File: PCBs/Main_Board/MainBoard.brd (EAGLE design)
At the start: 83.8 x 69.8 mm, 25 parts

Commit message: Minor changes to main board
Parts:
- moved USB_B 3.81 mm to (10.2, 57.1)
- moved USB_A 3.59 mm to (71.1, 61.0)
- moved R14 2.84 mm to (21.6, 52.1)
- moved R5 1.27 mm to (27.9, 24.1)
- moved 3.5MM 1.27 mm to (41.9, 59.7)
- flipped C1 to the top
- flipped C2 to the top
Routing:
- net GND: track 385.5 -> 360.5 mm
- net DAC_OUT: track 147.0 -> 154.2 mm
- net VCC_5: track 172.0 -> 177.9 mm
- net UART1_RX: track 59.3 -> 55.5 mm
- net LCD_MOSI: track 79.3 -> 75.6 mm
- net N$1: track 11.6 -> 14.8 mm
- net LCD_SCK: track 49.6 -> 46.9 mm
- net UART1_TX: track 60.9 -> 62.4 mm
- net LCD_CARD_CS: track 67.8 -> 66.3 mm
- net 3.5MM: track 20.8 -> 22.3 mm
- net LCD_MISO: track 58.9 -> 57.6 mm
- net N$6: track 3.81 -> 2.54 mm
- net ADDR_2: track 18.4 -> 17.4 mm

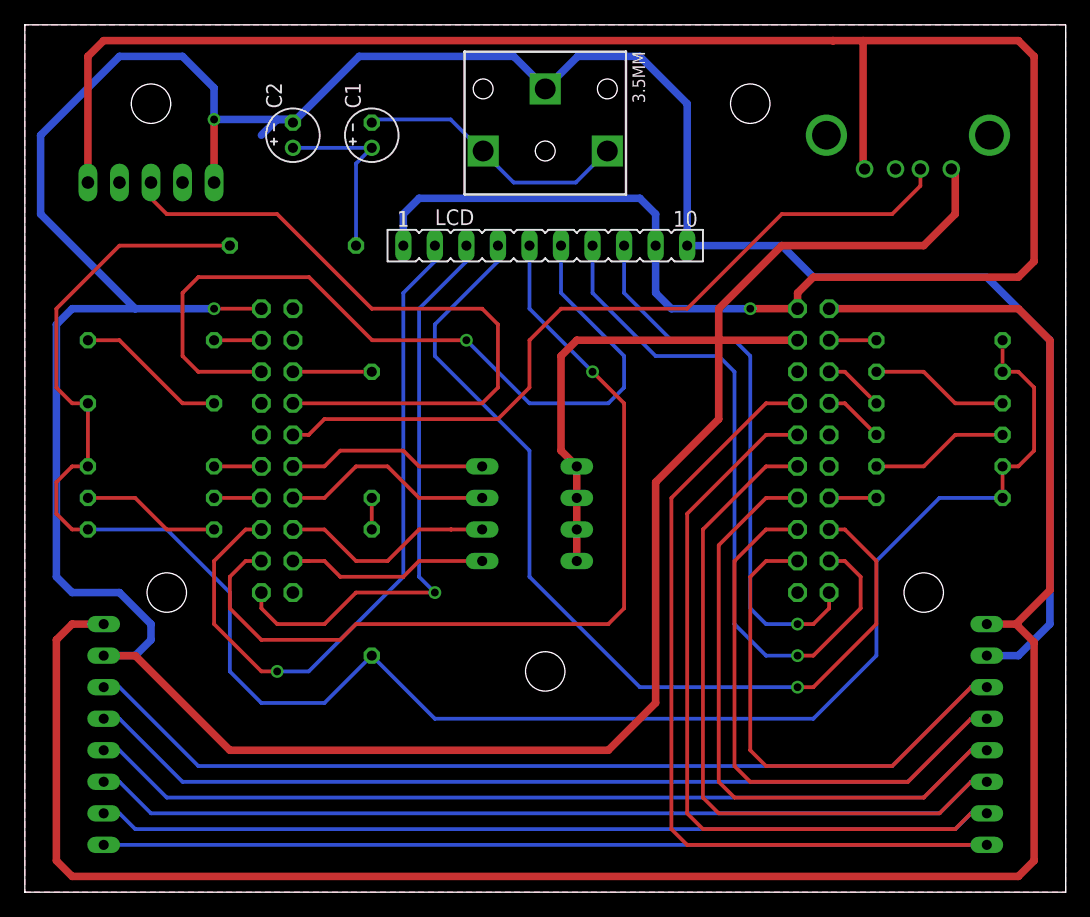
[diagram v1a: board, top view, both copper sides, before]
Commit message: Swapped D+/D- pins on the USB A port; misc optimizations
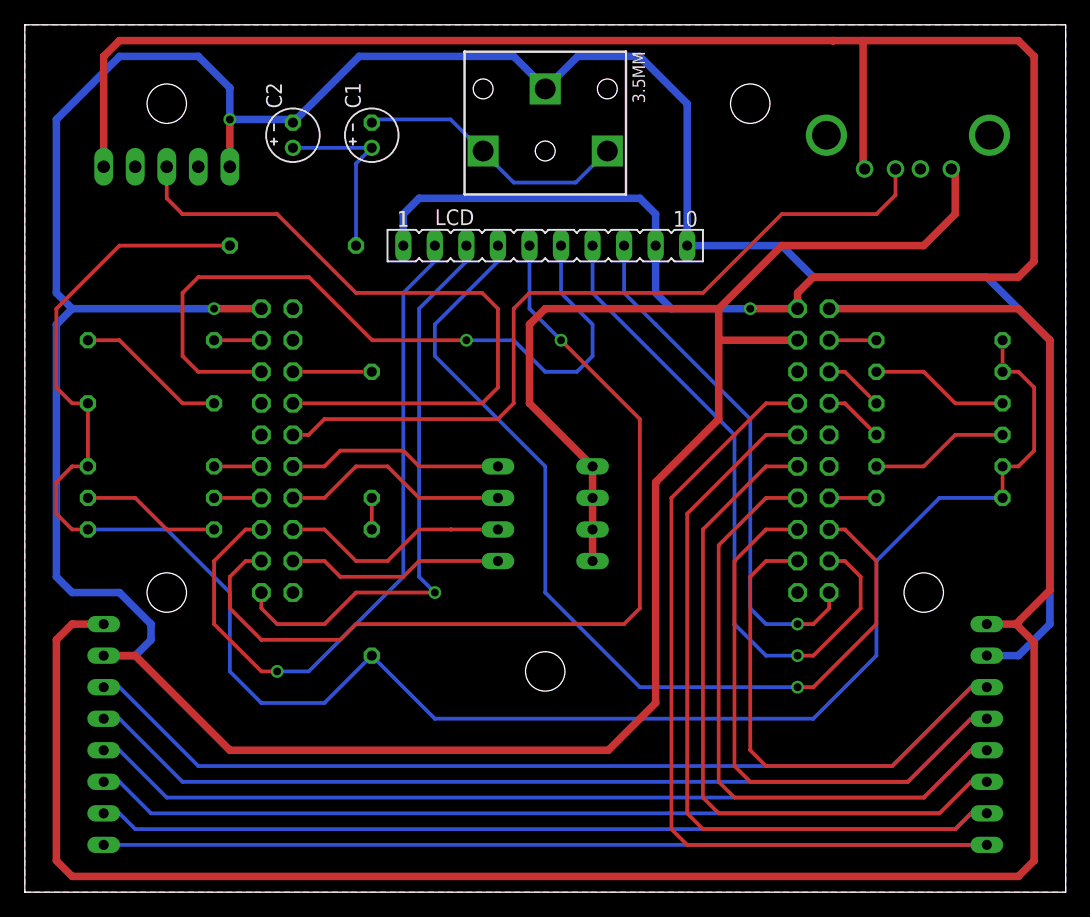
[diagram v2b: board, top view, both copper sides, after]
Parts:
- moved USB_B 1.80 mm to (11.4, 58.4)
- moved ADDR_SW 1.27 mm to (41.9, 30.5)
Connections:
- removed net N$67: USB_A.D-
- net UART1_TX: now also USB_A.D-; no longer USB_A.D+
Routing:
- net LCD_CARD_CS: track 66.3 -> 59.1 mm
- net LCD_D/C: track 56.6 -> 53.6 mm
- net LCD_RST: track 45.1 -> 42.1 mm
- net VCC_5: track 177.9 -> 175.4 mm
- net LCD_TFT_CS: track 71.8 -> 73.6 mm
- net ADDR_3: track 17.6 -> 18.8 mm
- net ADDR_1: track 17.3 -> 18.6 mm
- net ADDR_0: track 16.3 -> 17.6 mm
- net ADDR_2: track 17.4 -> 18.6 mm
- net UART1_RX: track 55.5 -> 56.3 mm
- net UART1_TX: track 62.4 -> 63.1 mm
- net GND: track 360.5 -> 359.9 mm

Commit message: Undid swap
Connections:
- net UART1_TX: now also USB_A.D+; no longer USB_A.D-
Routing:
- net UART1_TX: track 63.1 -> 65.4 mm
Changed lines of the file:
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@@
 <wire x1="54.61" y1="48.26" x2="60.96" y2="54.61" width="0.3048" layer="1"/>
 <wire x1="39.37" y1="39.37" x2="39.37" y2="46.99" width="0.3048" layer="1"/>
-<contactref element="USB_A" pad="D-"/>
-<wire x1="60.96" y1="54.61" x2="68.58" y2="54.61" width="0.3048" layer="1"/>
-<wire x1="68.58" y1="54.61" x2="70.1167" y2="56.1467" width="0.3048" layer="1"/>
-<wire x1="70.1167" y1="56.1467" x2="70.1167" y2="58.2422" width="0.3048" layer="1"/>
+<contactref element="USB_A" pad="D+"/>
+<wire x1="71.12" y1="54.61" x2="72.1233" y2="55.6133" width="0.3048" layer="1"/>
+<wire x1="72.1233" y1="55.6133" x2="72.1233" y2="58.2422" width="0.3048" layer="1"/>
+<wire x1="60.96" y1="54.61" x2="71.12" y2="54.61" width="0.3048" layer="1"/>
 </signal>
 <signal name="UART1_RX">
